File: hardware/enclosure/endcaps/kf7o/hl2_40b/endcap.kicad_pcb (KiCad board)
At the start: 2 copper layers, 106 x 40 mm, 39 parts, among them J2 Male Header, J3 Male Header, J4 Fan, Q1 DTC144E, Q2 IRLML6402, Q3 MULTIFET, Q4 MULTIFET, Q5 MULTIFET, Q6 MULTIFET, Q7 MULTIFET, U1 ACPL-M61M-500E

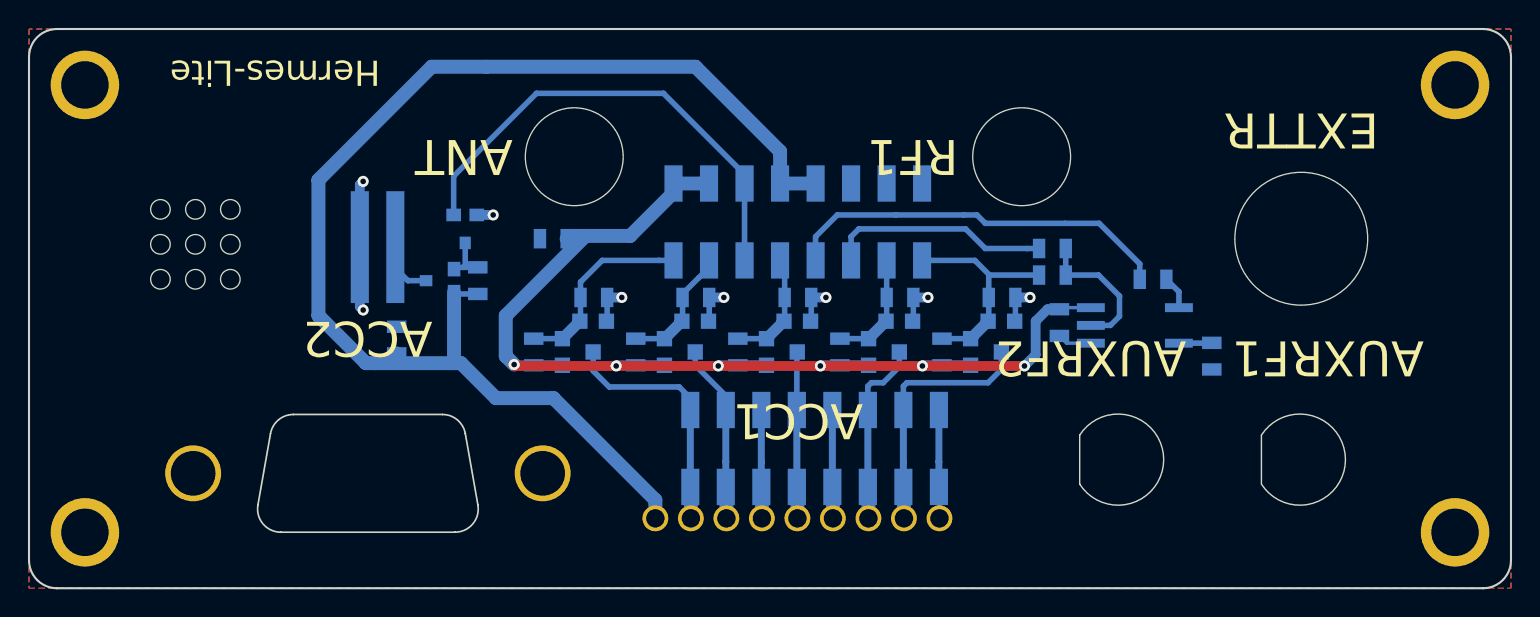
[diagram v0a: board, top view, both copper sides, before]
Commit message: Rear end plate 40mm 2.0
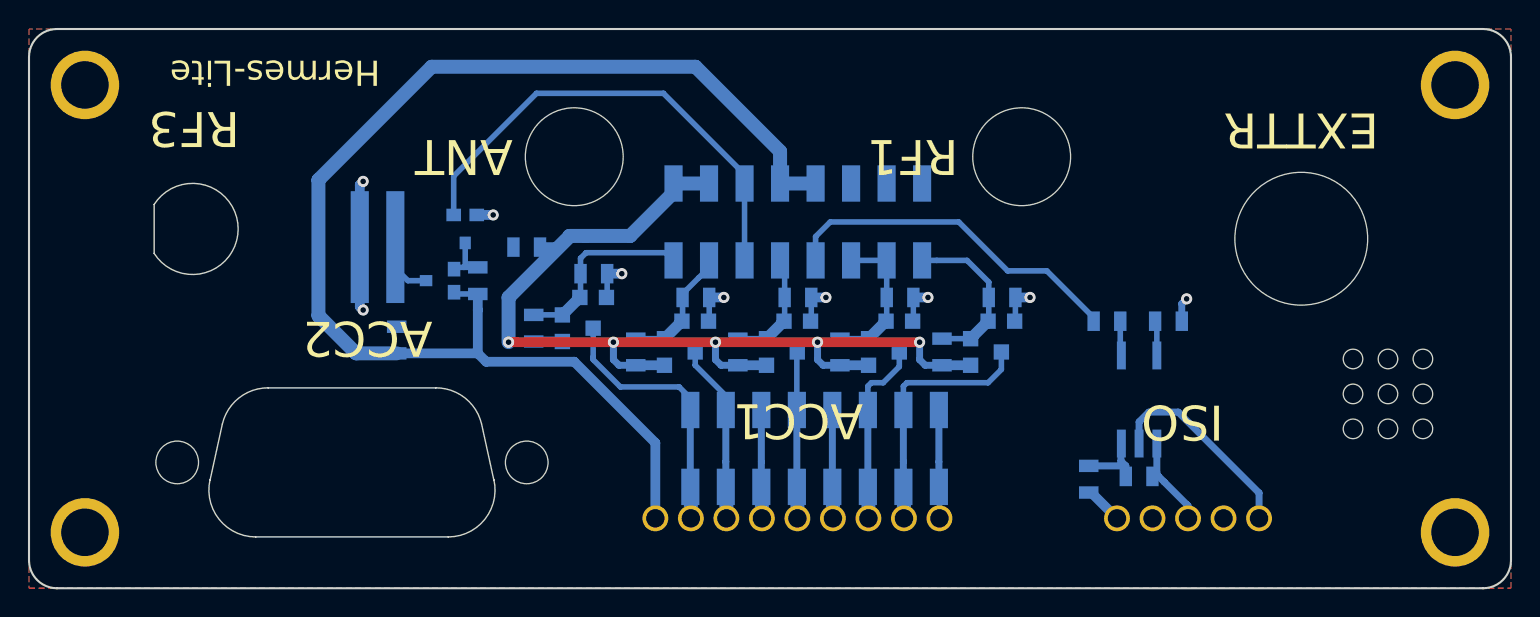
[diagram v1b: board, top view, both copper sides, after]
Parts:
- removed AUXRF1: SMA, endcaplib:sma_panel
- removed R14, R15: 0, endcaplib:SMD-0805
- added FB1: Ferrite_Bead_Small, endcaplib:SMD-0805, B.Cu at (125.8, 82.2)
- added ISO: Terminal Block, endcaplib:terminal_block5, B.Cu at (127.8, 85.0)
- ACC2: footprint endcaplib:DSUB-9_Cutout -> endcaplib:db9inside
- U1: value ACPL-M61M-500E -> ACPL-M21L-000E
- moved REF** 86.0 mm to (144.7, 78.6)
- moved RF3 68.2 mm to (61.7, 64.3)
- moved C1 12.4 mm to (129.4, 82.0), turned to 0 degrees
- moved U1 5.31 mm to (129.4, 76.5), turned to 270 degrees
- moved ACC2 4.92 mm to (73.1, 81.0)
- moved R12 4.46 mm to (127.1, 70.9)
- moved R13 3.98 mm to (131.5, 70.9), turned to 0 degrees
- moved C3 1.99 mm to (85.6, 65.6)
- moved Q3 1.70 mm to (91.3, 69.2)
- moved R3 1.70 mm to (90.4, 67.5)
- moved R2 1.70 mm to (86.1, 71.4)
- renumbered AUXRF2 to RF3
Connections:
- C1 pad 1: GNDS -> Net-(C1-Pad1)
- C1 pad 2: Vlvds -> Net-(C1-Pad2)
- J2 pad 14: Net-(J2-Pad14) -> Net-(J2-Pad12)
- Q6 pad 1: Net-(J2-Pad14) -> Net-(J2-Pad12)
- R8 pad 2: Net-(J2-Pad14) -> Net-(J2-Pad12)
- R9 pad 1: Net-(J2-Pad14) -> Net-(J2-Pad12)
- U1 pad 4: GNDS -> Net-(C1-Pad2)
- U1 pad 6: Vlvds -> Net-(C1-Pad1)
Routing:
- net Net-(J2-Pad14): track 9.39 -> 0.00 mm
- net Vlvds: track 85.9 -> 77.0 mm, vias 6 -> 5
- net Net-(C1-Pad2): track 0.00 -> 7.38 mm
- net Net-(C1-Pad1): track 0.00 -> 5.04 mm
- net Net-(ISO1-Pad5): track 10.1 -> 14.6 mm
- net Net-(J2-Pad12): track 16.0 -> 11.9 mm
- net Net-(J2-Pad16): track 18.1 -> 14.2 mm
- net ISOIN: track 28.1 -> 25.1 mm
- net Net-(FB1-Pad1): track 0.00 -> 2.79 mm
- net Net-(ACC1-Pad2): track 17.7 -> 19.0 mm
- net VSUP: track 91.7 -> 92.7 mm
- net GNDS: track 34.7 -> 33.9 mm, vias 8 -> 9
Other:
- board text added: "ISO"
- board text added: "RF3"
- board text removed: "AUXRF1"
- board text removed: "AUXRF2"

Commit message: Updates to endplate
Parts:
- moved REF** 85.1 mm to (60.3, 68.0)
- moved RF3 80.1 mm to (141.0, 75.3)
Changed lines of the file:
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@@
   (title_block
     (title "Hermes-Lite End Plate 40")
-    (date 2019-11-20)
+    (date 2019-11-23)
     (rev 2.0)
     (company SofterHardware)
@@
   )
   (setup
-    (last_trace_width 0.4)
+    (last_trace_width 0.25)
     (user_trace_width 0.2)
     (user_trace_width 0.4)
@@
   )
   (module endcaplib:sma_panel (layer B.Cu)
-    (at 61.7 64.3)
+    (at 141 75.3)
     (fp_text reference RF3 (at 0 4.5) (layer B.SilkS)
       (effects (font (size 1 1) (thickness 0.15)) (justify mirror))
@@
   )
   (module endcaplib:speakerventsmall (layer F.Cu)
-    (at 144.7 78.6)
+    (at 60.3 68)
     (fp_text reference REF** (at -1.1 3.9) (layer F.SilkS) hide
       (effects (font (size 1 1) (thickness 0.15)))
@@
     (effects (font (size 1.8 1.8) (thickness 0.2)))
   )
-  (gr_text RF3 (at 61.8 57.1 180) (layer F.SilkS)
-    (effects (font (size 2.5 2.5) (thickness 0.3)))
-  )
-  (gr_text ISO (at 132.5 78.1 180) (layer F.SilkS)
+  (gr_text RF3 (at 149.2 75.3 180) (layer F.SilkS)
+    (effects (font (size 2.5 2.5) (thickness 0.3)))
+  )
+  (gr_text ISO (at 132 78 180) (layer F.SilkS)
     (effects (font (size 2.5 2.5) (thickness 0.3)))
   )
@@
     (effects (font (size 2.5 2.5) (thickness 0.3)))
   )
-  (gr_text RF3 (at 68.3 64.2 270) (layer Eco1.User)
+  (gr_text RF3 (at 149 75.7 270) (layer Eco1.User)
     (effects (font (size 2.5 2.5) (thickness 0.3)))
   )
@@
     (effects (font (size 2.5 2.5) (thickness 0.3)))
   )
-  (gr_text EXTTR (at 149 65 270) (layer Eco1.User)
-    (effects (font (size 2.5 2.5) (thickness 0.3)))
-  )
+  (gr_text EXTTR (at 149 64.5 270) (layer Eco1.User)
+    (effects (font (size 2.5 2.5) (thickness 0.3)))
+  )

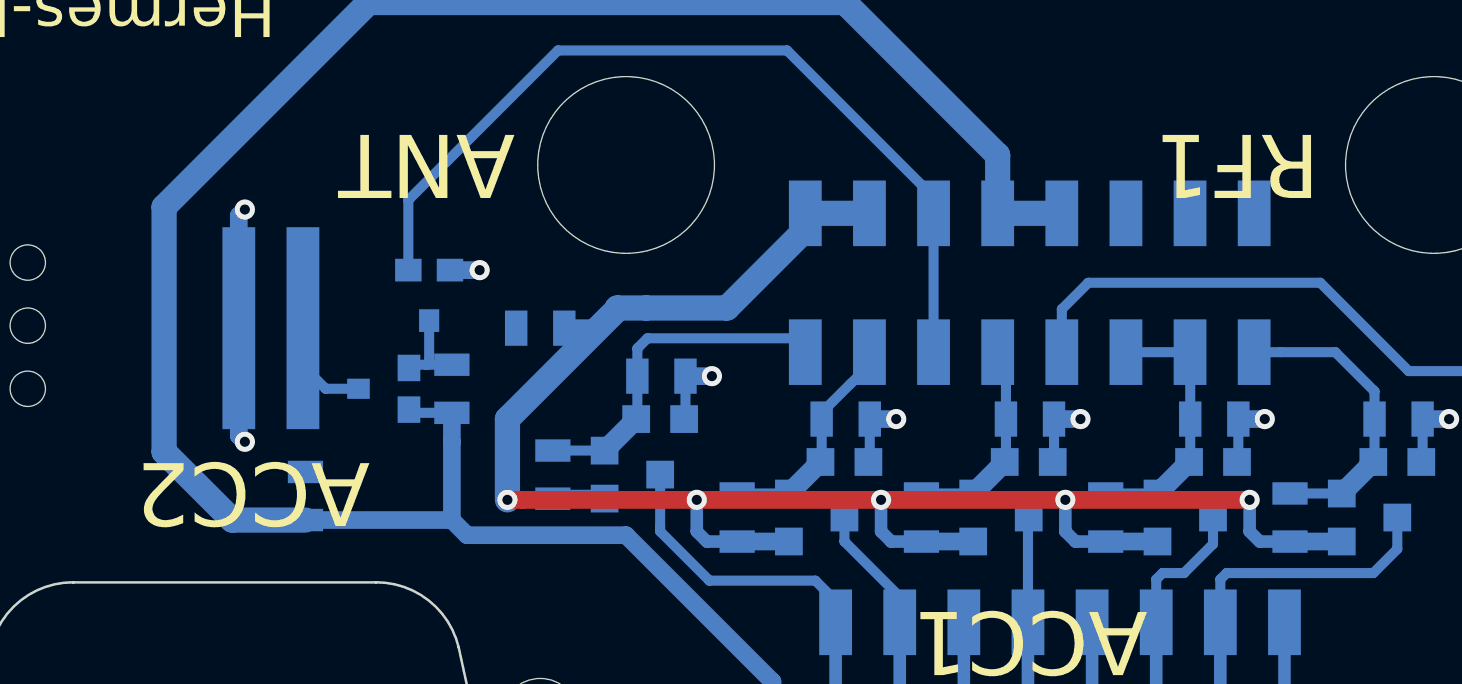
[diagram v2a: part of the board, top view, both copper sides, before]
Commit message: 55mm rev2 endplate
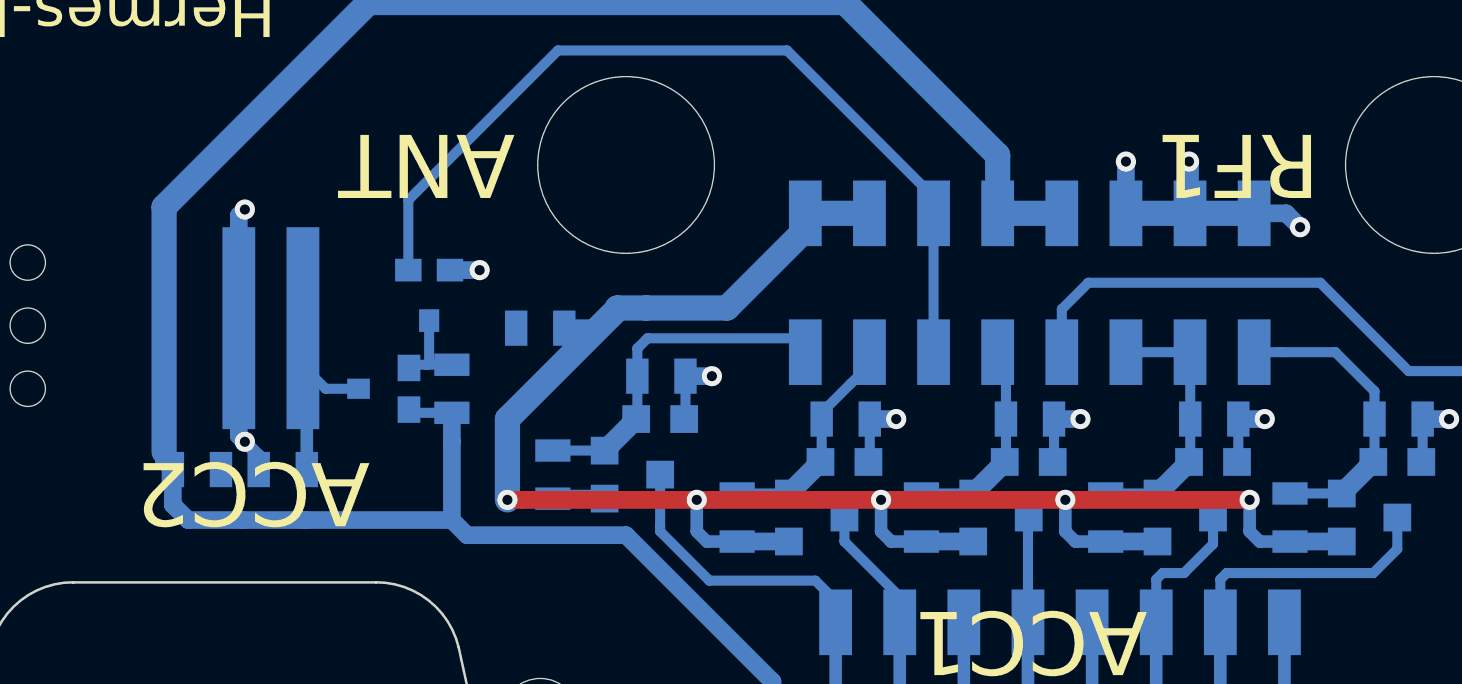
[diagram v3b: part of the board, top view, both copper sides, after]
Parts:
- added C4: 0.1uF, endcaplib:SMD-0805, B.Cu at (75.4, 71.2)
- moved C2 4.43 mm to (72.0, 71.2), turned to 180 degrees
- renumbered ISO to ISO1
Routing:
- net GNDS: track 33.9 -> 46.5 mm, vias 9 -> 12
- net Net-(C4-Pad2): track 4.07 -> 9.74 mm
- net VSUP: track 92.7 -> 93.7 mm

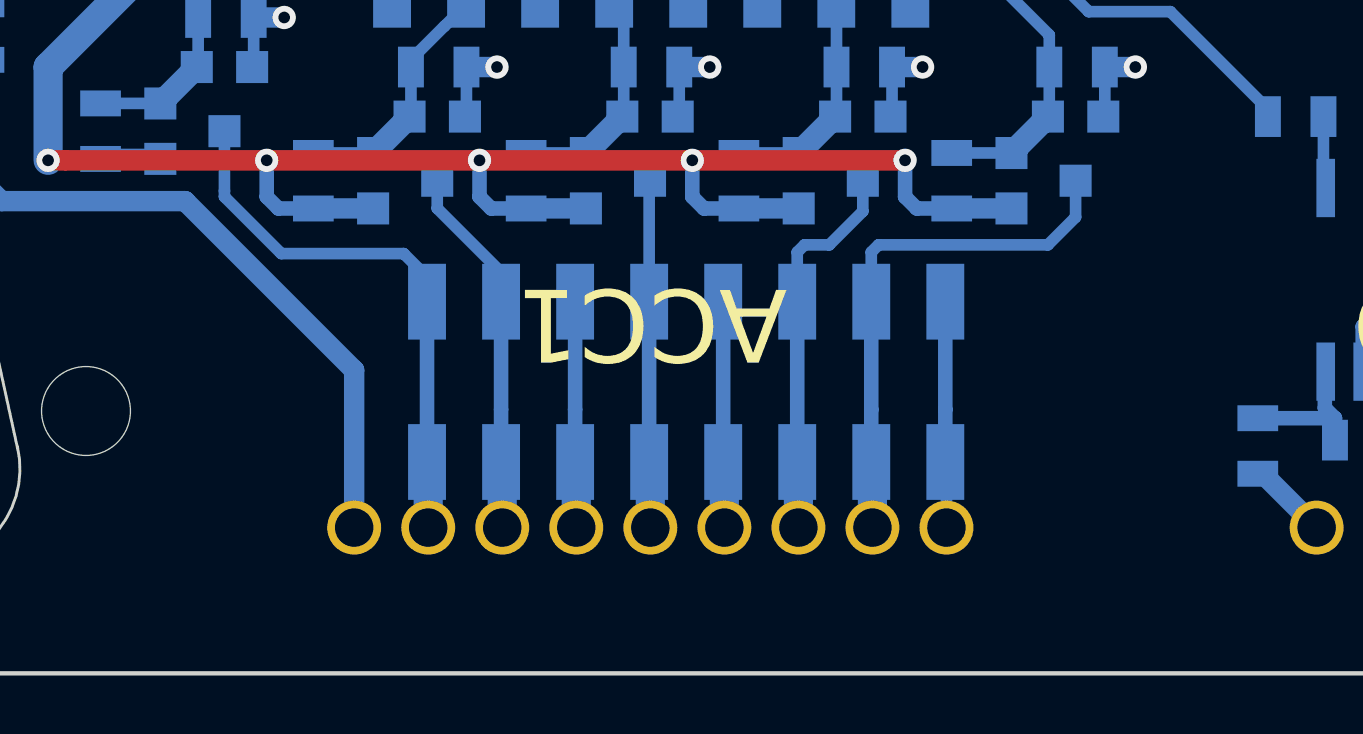
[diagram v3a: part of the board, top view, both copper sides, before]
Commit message: Added pullups, diodes to some channels
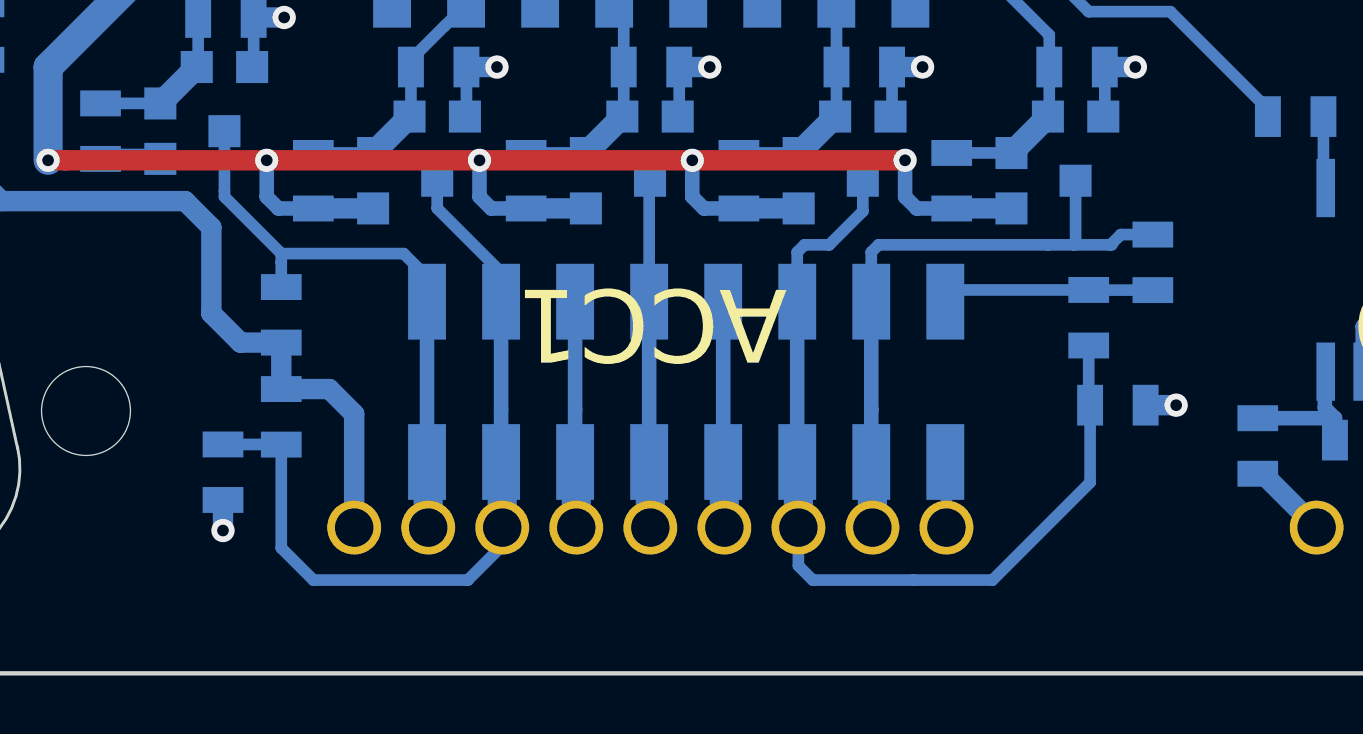
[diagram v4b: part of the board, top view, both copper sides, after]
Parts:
- added D1: 1N4148, endcaplib:SMD-0805, B.Cu at (121.0, 80.8)
- added D2: 1N4148, endcaplib:SMD-0805, B.Cu at (90.3, 83.1)
- added R14: 10K, endcaplib:SMD-0805, B.Cu at (122.2, 75.9)
- added R15: 10K, endcaplib:SMD-0805, B.Cu at (120.0, 77.8)
- added R16: 10K, endcaplib:SMD-0805, B.Cu at (92.3, 81.2)
- added R17: 10K, endcaplib:SMD-0805, B.Cu at (92.3, 77.7)
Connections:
- J3 pad 15: GNDS -> Net-(J3-Pad15)
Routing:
- net Net-(ACC1-Pad7): track 13.3 -> 31.0 mm
- net Net-(ACC1-Pad3): track 12.8 -> 27.5 mm
- net Net-(J3-Pad15): track 0.00 -> 7.29 mm
- net Net-(ACC1-Pad8): track 18.2 -> 21.6 mm
- net GNDS: track 46.5 -> 43.1 mm, vias 12 -> 14
- net VSUP: track 93.7 -> 95.5 mm
- net Net-(ACC1-Pad2): track 19.0 -> 20.0 mm
